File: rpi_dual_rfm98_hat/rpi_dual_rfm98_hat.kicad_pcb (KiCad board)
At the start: 2 copper layers, 65 x 56 mm, 17 parts, among them J1 Conn_01x02_Male, J2 Conn_Coaxial, J3 Conn_Coaxial, J4 Conn_01x03_Male, P1 Conn_02x20_Odd_Even, U1 RFM98PW-symbols, U2 RFM98PW-symbols

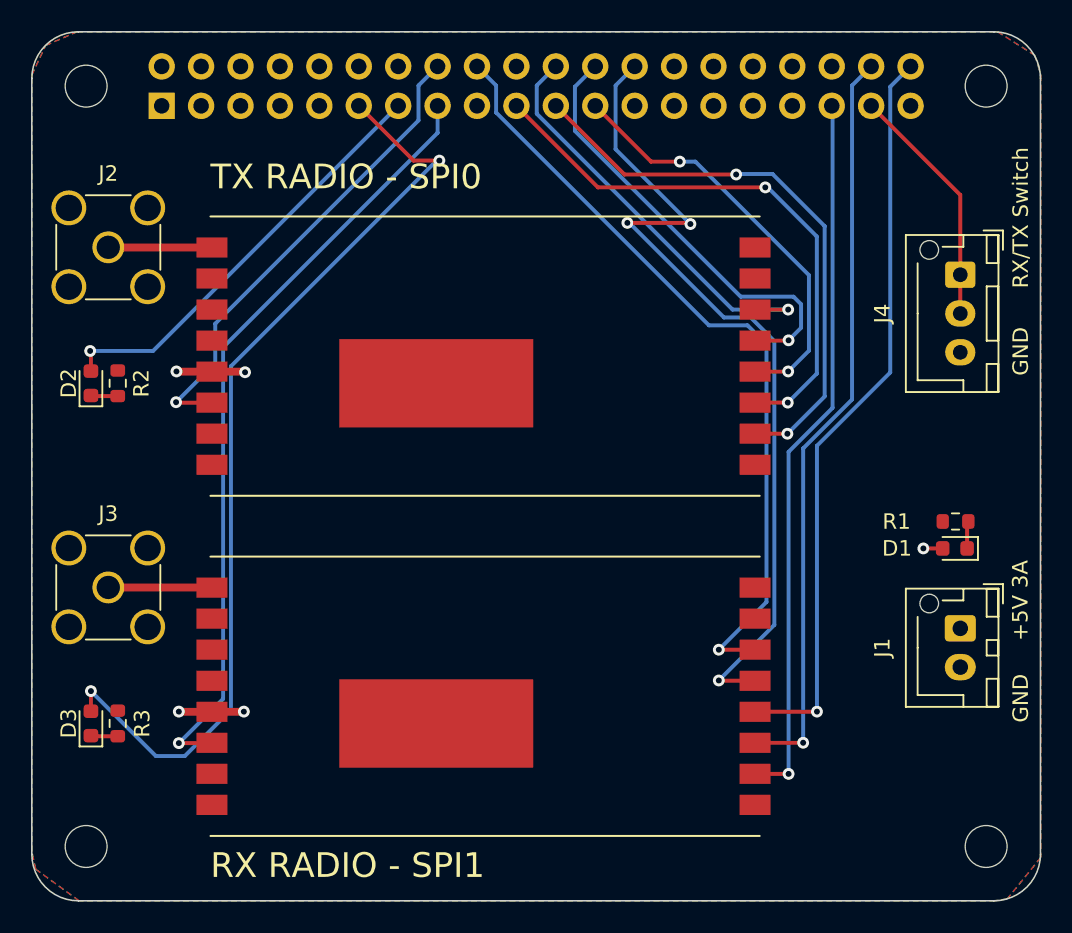
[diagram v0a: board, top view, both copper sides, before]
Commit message: Re-mapped SPI1 CE pin
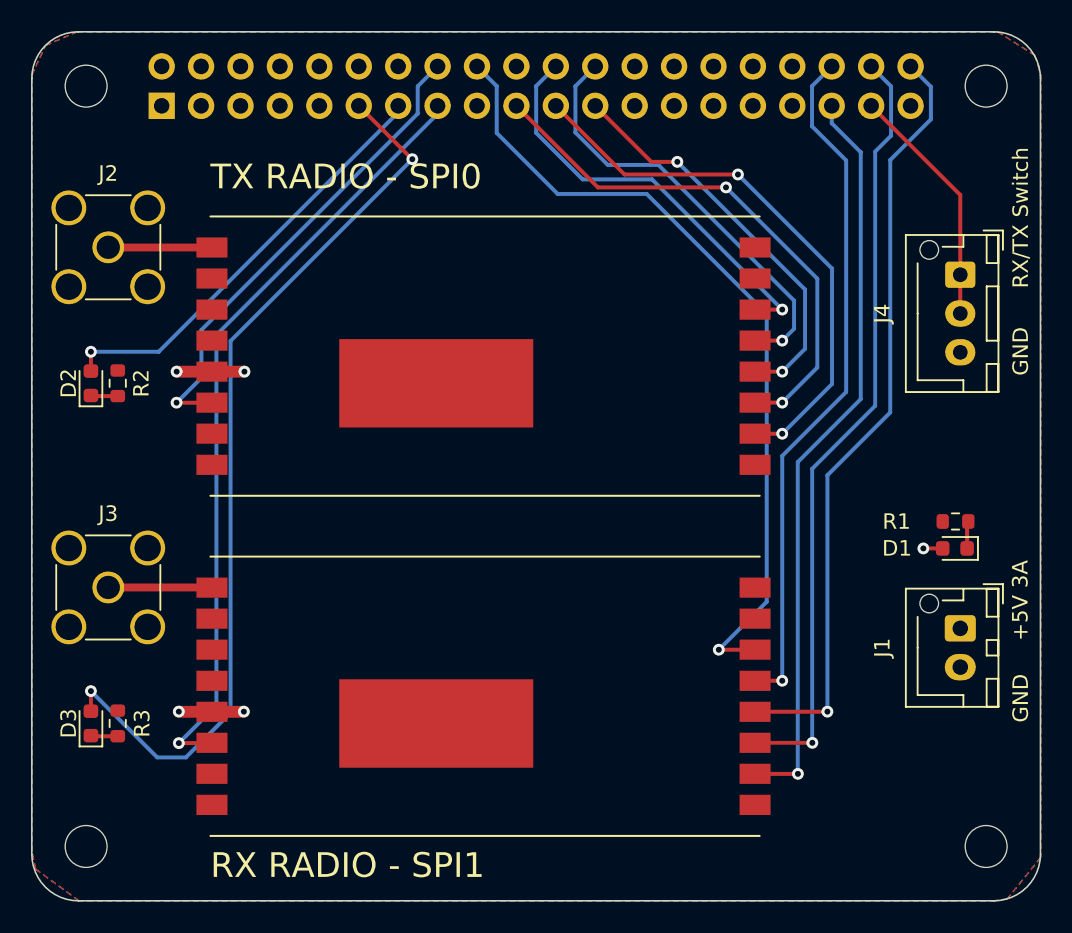
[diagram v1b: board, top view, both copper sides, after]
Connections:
- P1 pad 26: /GPIO7(SPI1_CE_N) -> /GPIO7
- P1 pad 36: /GPIO16 -> /GPIO16(SPI1_CE_N)
- U2 pad 13: /GPIO7(SPI1_CE_N) -> /GPIO16(SPI1_CE_N)
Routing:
- net /GPIO7(SPI1_CE_N): track 55.1 -> 0.00 mm, vias 3 -> 0
- net /GPIO16(SPI1_CE_N): track 0.00 -> 44.5 mm, vias 0 -> 1
- net /GPIO17(GEN0): track 61.0 -> 58.7 mm
- net /GPIO24(GEN5): track 50.4 -> 52.3 mm
- net /GPIO19(SPI1_MISO): track 46.4 -> 48.3 mm
- net /GPIO10(SPI0_MOSI): track 36.4 -> 34.7 mm
- net /GPIO21(SPI1_SCK): track 48.1 -> 49.5 mm
- net /GPIO20(SPI1_MOSI): track 48.5 -> 49.9 mm
- net /GPIO9(SPI0_MISO): track 37.0 -> 35.9 mm
- net /GPIO11(SPI0_SCK): track 27.2 -> 26.1 mm
- net /GPIO8(SPI0_CE_N): track 28.7 -> 28.0 mm
- net /GPIO22(GEN3): track 50.1 -> 49.6 mm

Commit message: add CS pullups, ground under antenna connectors
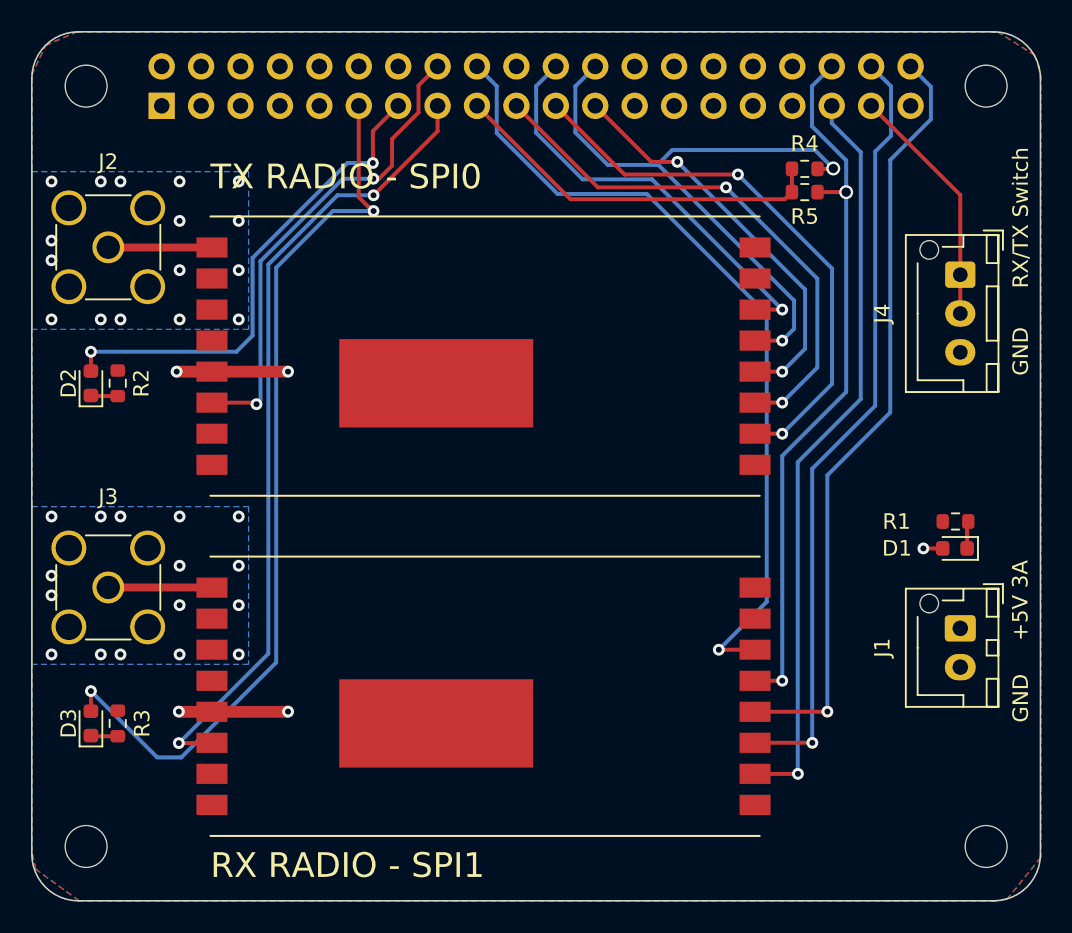
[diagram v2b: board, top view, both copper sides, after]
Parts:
- added R4: 10K, Resistor_SMD:R_0603_1608Metric, F.Cu at (249.8, 102.8)
- added R5: 10K, Resistor_SMD:R_0603_1608Metric, F.Cu at (249.8, 104.3)
- D1: value LED -> RED
- D2, D3: value LED -> GREEN
- R1: value R_US -> 330
- R2, R3: value R_US -> 470
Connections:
- P1 pad 17: unconnected-(P1-Pad17) -> +3V3
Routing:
- net +3V3: track 0.00 -> 24.5 mm
- net /GPIO8(SPI0_CE_N): track 28.0 -> 41.3 mm, vias 1 -> 2
- net +5V: track 9.81 -> 15.5 mm
- net /GPIO27(GEN2): track 27.4 -> 31.7 mm, vias 1 -> 2
- net /GPIO22(GEN3): track 49.6 -> 51.5 mm, vias 1 -> 2
- net /GPIO16(SPI1_CE_N): track 44.5 -> 46.3 mm, vias 1 -> 2
- net /GPIO17(GEN0): track 58.7 -> 58.0 mm
- net /GPIO23(GEN4): vias 1 -> 2
- net GND: vias 0 -> 32
- added copper zone on B.Cu, net GND
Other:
- board text added: "TX RADIO - SPI0 CS: GPIO8 RESET: GPIO25 GPIO_0: GPIO23 TX LED: GPIO27 RX RADIO - SPI1 CS: GPIO16 RESET: GPIO24 GPIO_0: GPIO22 RX LED: GPIO17 RX/TX Switch: GPIO26"
- board text removed: "TX RADIO - SPI0 CS: GPIO8 RESET: GPIO25 GPIO_0: GPIO23 TX LED: GPIO27 RX RADIO - SPI1 CS: GPIO21 RESET: GPIO24 GPIO_0: GPIO22 RX LED: GPIO17 RX/TX Switch: GPIO26"

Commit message: Minor changes
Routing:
- net /GPIO22(GEN3): track 51.5 -> 53.6 mm
- net /GPIO17(GEN0): track 58.0 -> 59.3 mm
- net +5V: track 15.5 -> 16.5 mm
- net /GPIO27(GEN2): track 31.7 -> 32.7 mm

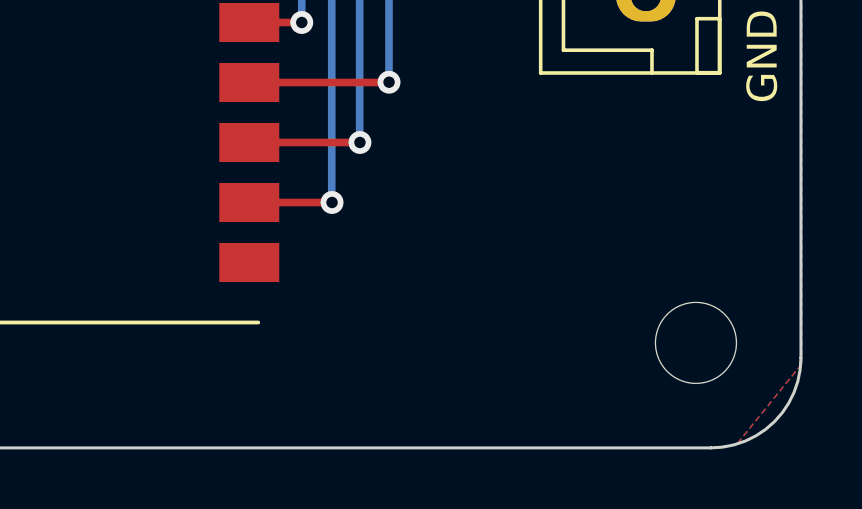
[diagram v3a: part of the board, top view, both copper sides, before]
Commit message: Added the fan connector
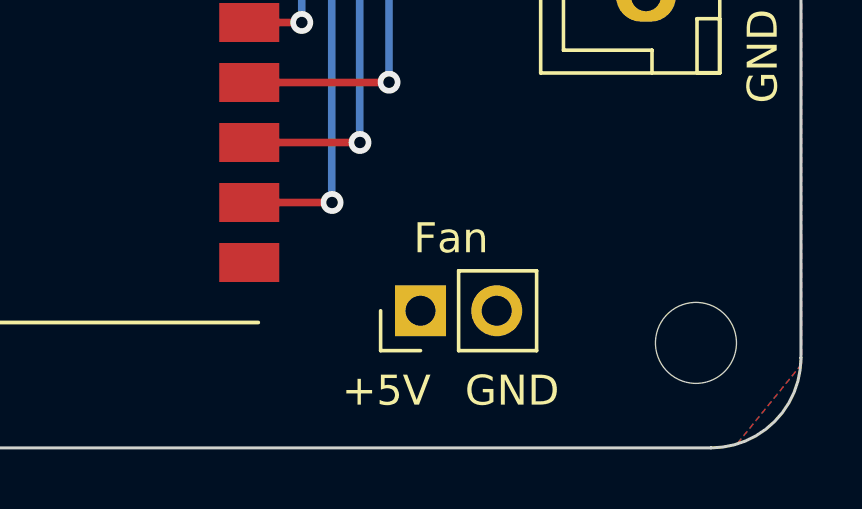
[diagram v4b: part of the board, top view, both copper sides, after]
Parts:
- added Fan: Conn_01x02_Male, Connector_PinHeader_2.54mm:PinHeader_1x02_P2.54mm_Vertical, F.Cu at (252.3, 145.4)
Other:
- board text added: "+5V"
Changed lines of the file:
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@@
+    )
+  )
+  (footprint "Connector_PinHeader_2.54mm:PinHeader_1x02_P2.54mm_Vertical" (layer "F.Cu")
+    (at 252.319006 145.428005 90)
+    (descr "Through hole straight pin header, 1x02, 2.54mm pitch, single row")
+    (tags "Through hole pin header THT 1x02 2.54mm single row")
+    (property "Sheetfile" "rpi_dual_rfm98_hat.kicad_sch")
+    (property "Sheetname" "")
+    (attr through_hole)
+    (fp_text reference "Fan" (at 2.413 1.016 180) (layer "F.SilkS")
+      (effects (font (size 1 1) (thickness 0.15)))
+    )
+    (fp_text value "Conn_01x02_Male" (at 0 4.87 90) (layer "F.Fab")
+      (effects (font (size 1 1) (thickness 0.15)))
+    )
+    (fp_text user "${REFERENCE}" (at 0 1.27) (layer "F.Fab")
+      (effects (font (size 1 1) (thickness 0.15)))
+    )
+    (fp_line (start -1.33 0) (end -1.33 -1.33) (layer "F.SilkS") (width 0.12))
+    (fp_line (start -1.33 -1.33) (end 0 -1.33) (layer "F.SilkS") (width 0.12))
+    (fp_line (start -1.33 1.27) (end -1.33 3.87) (layer "F.SilkS") (width 0.12))
+    (fp_line (start 1.33 1.27) (end 1.33 3.87) (layer "F.SilkS") (width 0.12))
+    (fp_line (start -1.33 1.27) (end 1.33 1.27) (layer "F.SilkS") (width 0.12))
+    (fp_line (start -1.33 3.87) (end 1.33 3.87) (layer "F.SilkS") (width 0.12))
+    (fp_line (start 1.8 4.35) (end 1.8 -1.8) (layer "F.CrtYd") (width 0.05))
+    (fp_line (start -1.8 4.35) (end 1.8 4.35) (layer "F.CrtYd") (width 0.05))
+    (fp_line (start 1.8 -1.8) (end -1.8 -1.8) (layer "F.CrtYd") (width 0.05))
+    (fp_line (start -1.8 -1.8) (end -1.8 4.35) (layer "F.CrtYd") (width 0.05))
+    (fp_line (start -1.27 3.81) (end -1.27 -0.635) (layer "F.Fab") (width 0.1))
+    (fp_line (start 1.27 3.81) (end -1.27 3.81) (layer "F.Fab") (width 0.1))
+    (fp_line (start -0.635 -1.27) (end 1.27 -1.27) (layer "F.Fab") (width 0.1))
+    (fp_line (start 1.27 -1.27) (end 1.27 3.81) (layer "F.Fab") (width 0.1))
+    (fp_line (start -1.27 -0.635) (end -0.635 -1.27) (layer "F.Fab") (width 0.1))
+    (pad "1" thru_hole rect (at 0 0 90) (size 1.7 1.7) (drill 1) (layers *.Cu *.Mask)
+      (net 1 "+5V") (pinfunction "Pin_1") (pintype "passive"))
+    (pad "2" thru_hole oval (at 0 2.54 90) (size 1.7 1.7) (drill 1) (layers *.Cu *.Mask)
+      (net 2 "GND") (pinfunction "Pin_2") (pintype "passive"))
+    (model "${KICAD6_3DMODEL_DIR}/Connector_PinHeader_2.54mm.3dshapes/PinHeader_1x02_P2.54mm_Vertical.wrl"
+      (offset (xyz 0 0 0))
+      (scale (xyz 1 1 1))
+      (rotate (xyz 0 0 0))
     )
   )
@@
     (effects (font (size 0.762 0.762) (thickness 0.127)) (justify left mirror))
   )
+  (gr_text "+5V\n" (at 251.181006 148.095005) (layer "F.SilkS")
+    (effects (font (size 1 1) (thickness 0.1524)))
+  )
   (gr_text "GND" (at 263.728708 136.944405 90) (layer "F.SilkS")
     (effects (font (size 1 1) (thickness 0.1524)))
@@
     (effects (font (size 1 1) (thickness 0.1524)))
   )
+  (gr_text "GND" (at 255.372006 148.095005) (layer "F.SilkS")
+    (effects (font (size 1 1) (thickness 0.1524)))
+  )
